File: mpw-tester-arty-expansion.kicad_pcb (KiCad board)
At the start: 4 copper layers, 53.3 x 61.5 mm, 140 parts, among them J1 USB4105-GF-A, J10 61300211121, J11 61300211121, J12 61300211121, J14 61300311121, J15 61300311121, J18 61300411121, J19 61300711121, J2 61300211121, J20 61300411121, J3 Arty_A7_SPI, J4 61300211121, J5 61300311121, J6 61300211121, J7 61300211121, J8 61300211121, J9 61300211121, Q1 DTC014TEBTL, U1 SN74LVC1G125DCKR, U2 FT232HQ, U3 SN74LVC1G125DCKR, U4 MAX811REUS+T, U5 NTS0102DP, U6 MCP4661-103E/ML, U7 Caravel_breakout_PCB, U8 W25Q32FVSS, U9 MIC2211-AAYML-TR, Y1 ABM8G-12.000MHZ-18-D2Y-T, Y2 ECS-2520MVLC-100-BN-TR

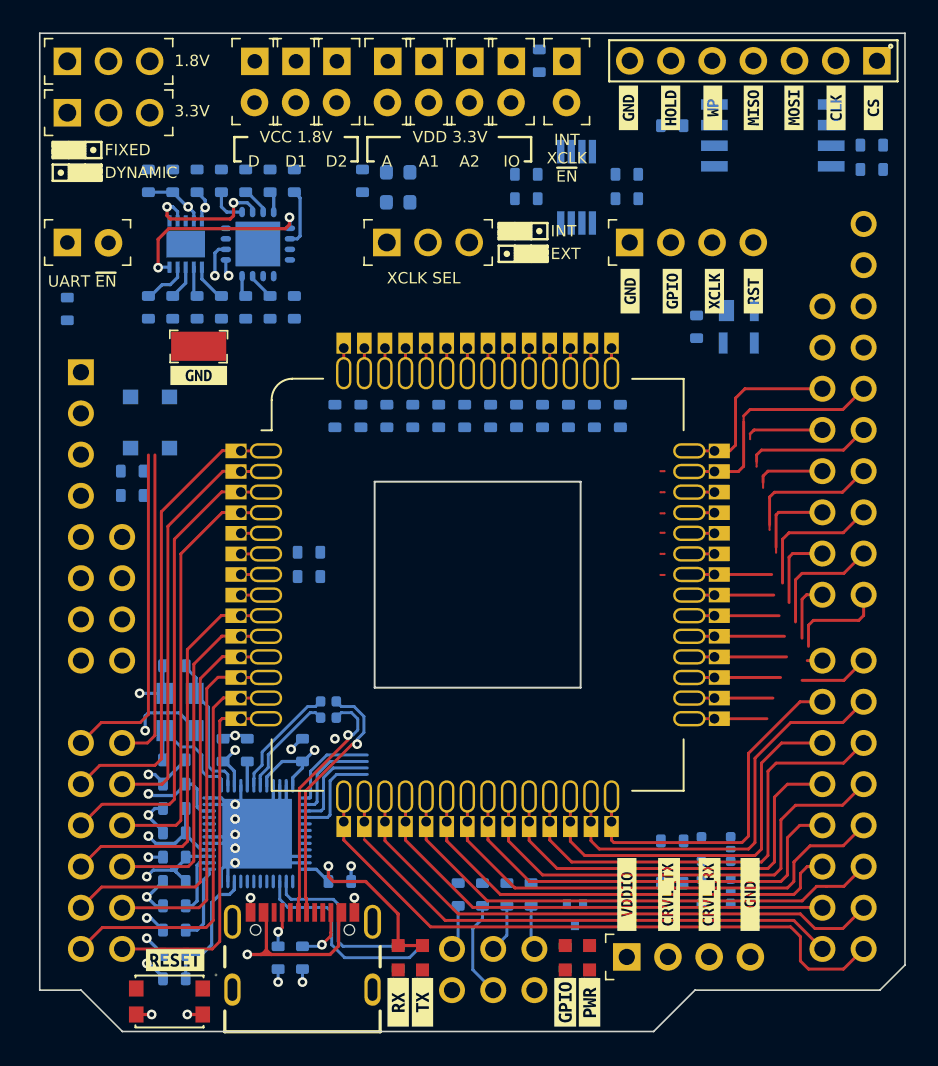
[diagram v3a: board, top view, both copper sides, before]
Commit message: Start power section layout. Adjust J6-J12 position on schematic to resolve crosses on PCB
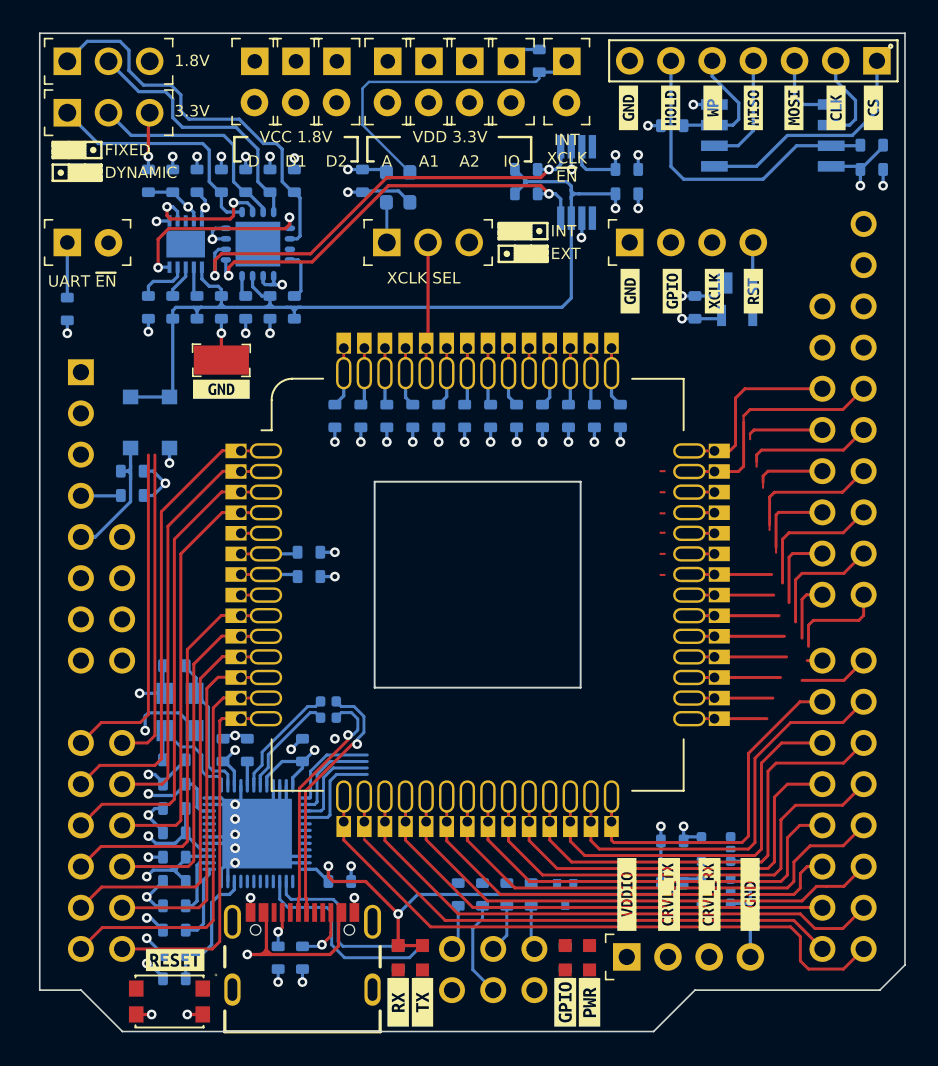
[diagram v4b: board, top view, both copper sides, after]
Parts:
- moved U4 1.70 mm to (166.0, 82.4)
- moved TP1 1.64 mm to (134.2, 86.2)
- moved kibuzzard-638FA1CB 1.64 mm to (134.2, 88.0)
- moved Q1 1.39 mm to (155.4, 119.1)
- moved C20 1.20 mm to (163.4, 82.9)
- moved C21 0.30 mm to (159.2, 74.4)
- moved C25 0.30 mm to (159.2, 75.9)
- moved R27 0.30 mm to (153.0, 74.4)
- moved R31 0.30 mm to (153.0, 75.9)
- moved U5 0.30 mm to (156.1, 75.2)
- turned C19 to -90 degrees
- turned R16 to 90 degrees
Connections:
- J3 pad 19: unconnected-(J3-Pad19) -> /EN_VOUT2
- J3 pad 31: unconnected-(J3-Pad31) -> /~{MR}
- J3 pad 32: unconnected-(J3-Pad32) -> /ARTY_XCLK
- J3 pad 9: unconnected-(J3-Pad9) -> /EN_VOUT1
- J6 pad 2: /VDDIO -> /VDDA
- J7 pad 2: /VDDA -> /VDDIO
- J8 pad 2: /VDDA1 -> /VDDA2
- J9 pad 2: /VDDA2 -> /VDDA1
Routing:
- net /3V3_ARTY: track 0.00 -> 56.9 mm, vias 0 -> 2
- net /5V0: track 4.03 -> 59.5 mm, vias 0 -> 1
- net AGND: track 74.4 -> 125.3 mm, vias 23 -> 52
- net /ARTY_SDA: track 2.17 -> 28.7 mm, vias 1 -> 2
- net VBUS: track 30.3 -> 56.6 mm, vias 2 -> 3
- net /ARTY_SCL: track 1.05 -> 26.3 mm, vias 1 -> 2
- net +3V3: track 2.06 -> 23.0 mm, vias 1 -> 13
- net unconnected-(J3-Pad9): track 20.9 -> 0.00 mm
- net /EN_VOUT1: track 1.86 -> 22.7 mm
- net /P0B: track 3.54 -> 24.4 mm
- net /XCLK_EN: track 0.00 -> 19.9 mm
- net /VDDIO: track 3.10 -> 22.9 mm
- net /FTDI_3V3: track 33.5 -> 53.1 mm, vias 6 -> 7
- net unconnected-(J3-Pad19): track 19.5 -> 0.00 mm
- net /EN_VOUT2: track 2.11 -> 21.6 mm
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- added copper zone on In2.Cu, net +1V8
- added copper zone on In2.Cu, net +3V3

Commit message: Import changes to PCB, place new diodes
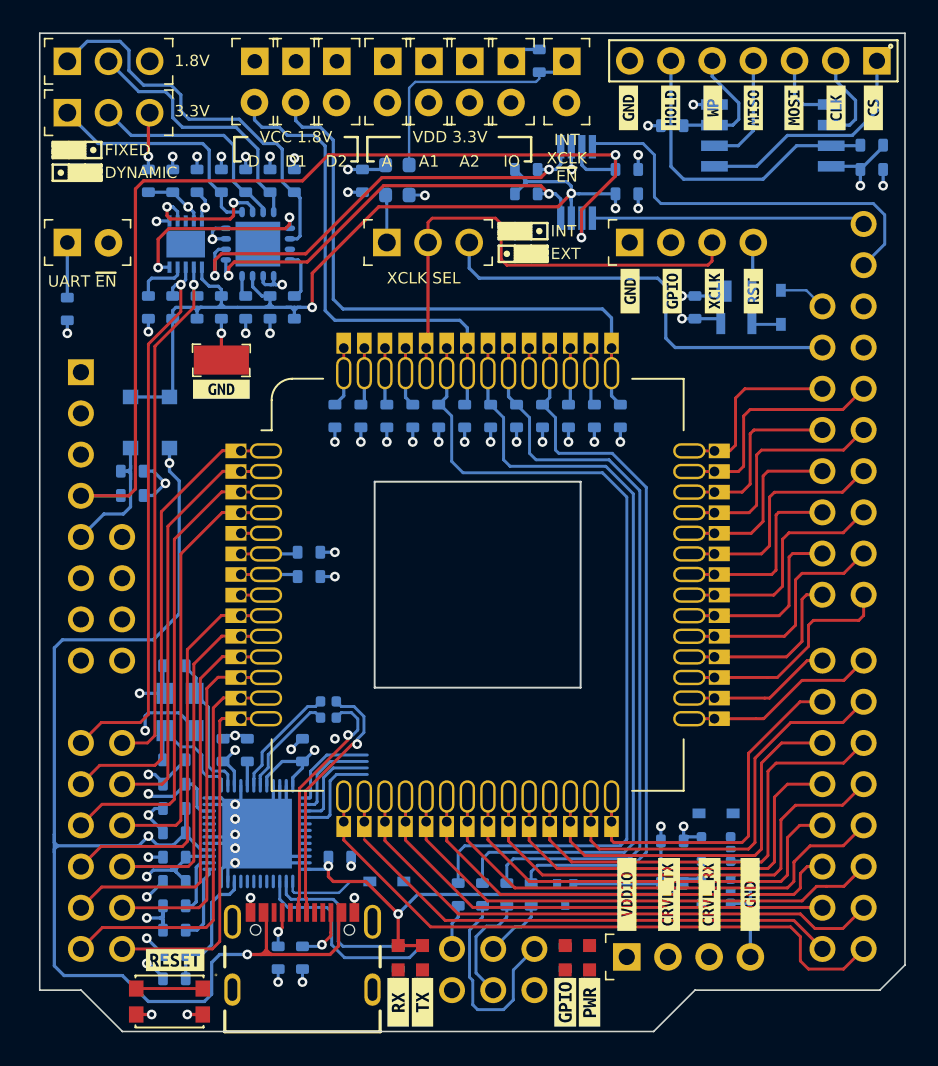
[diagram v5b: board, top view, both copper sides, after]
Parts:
- removed NT1, NT10, NT11, NT12, NT2, NT3, NT4, NT5, NT6, NT7, NT8, NT9: NetTie_2, antmicro-footprints:NetTie-2_SMD_Pad0.127mm
- added D7: 1N5819HW-7-F, antmicro-footprints:SOD-123, B.Cu at (131.0, 90.0)
- added D8: 1N5819HW-7-F, antmicro-footprints:SOD-123, B.Cu at (128.6, 90.0)
- added D9: PMEG6002EJ,115, antmicro-footprints:SOD-323F, B.Cu at (168.7, 82.9)
- D5, D6: value 1N5819HW-7-F -> PMEG6002EJ,115; footprint antmicro-footprints:SOD-123 -> antmicro-footprints:SOD-323F
- moved D5 41.4 mm to (164.7, 114.1), turned to 0 degrees
- moved D6 32.4 mm to (144.4, 118.3), turned to 0 degrees
- moved R14 3.00 mm to (150.3, 119.1)
- moved C16 1.50 mm to (141.5, 116.8)
- moved R11 1.50 mm to (153.3, 119.1)
- moved R15 1.50 mm to (151.8, 119.1)
- moved U4 0.50 mm to (165.9, 82.9)
- moved Y2 0.45 mm to (145.1, 75.0)
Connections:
- D5 pad A: VBUS -> /~{UART_EN}
- D5 pad K: /5V0 -> Net-(U2-Pad21)
- D6 pad A: /5V0_ARTY -> /~{MR}
- D6 pad K: /5V0 -> Net-(U2-Pad25)
- J18 pad 2: /CRVL_TX -> /CRVL_IO5
- J18 pad 3: /CRVL_RX -> /CRVL_IO6
- J3 pad 19: /EN_VOUT2 -> /EN_VOUT1
- J3 pad 31: /~{MR} -> Net-(J3-Pad31)
- J3 pad 34: /ARTY_MOSI -> /CRVL_IO2
- J3 pad 35: /ARTY_SCK -> /CRVL_IO4
- J3 pad 36: /ARTY_RX -> /CRVL_IO6
- J3 pad 51: /ARTY_MISO -> /CRVL_IO1
- J3 pad 52: /ARTY_CS -> /CRVL_IO3
- J3 pad 53: /ARTY_TX -> /CRVL_IO5
- J3 pad 9: /EN_VOUT1 -> /EN_VOUT2
- Q1 pad 1: /GPIO -> /CRVL_GPIO
- U2 pad 13: /USB_SCK_TXD -> /CRVL_IO4
- U2 pad 14: /USB_SO_RXD -> /CRVL_IO2
- U2 pad 15: /USB_SI -> /CRVL_IO1
- U2 pad 16: /USB_CS1 -> /CRVL_IO3
- U2 pad 21: /~{UART_EN} -> Net-(U2-Pad21)
- U2 pad 25: /~{MR} -> Net-(U2-Pad25)
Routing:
- net /MEM.~{CS}: track 18.2 -> 67.5 mm
- net /MEM.SI: track 8.19 -> 53.5 mm
- net /MEM.SO: track 10.8 -> 53.7 mm
- net /MEM.SCK: track 9.43 -> 49.9 mm
- net /VCCD1: track 3.72 -> 36.9 mm
- net /ARTY_XCLK: track 0.00 -> 27.3 mm
- net /VCCD: track 7.10 -> 33.8 mm
- net /ARTY_SDA_3V3: track 0.00 -> 25.1 mm
- net /VDDA1: track 3.58 -> 27.3 mm
- net /CRVL_XCLK: track 8.11 -> 30.7 mm
- net VBUS: track 56.6 -> 79.1 mm
- net /CRVL_IO3: track 1.55 -> 20.9 mm
- net /VDDA: track 3.54 -> 21.8 mm
- net /VDDIO: track 22.9 -> 40.3 mm
- net /ARTY_SCL_3V3: track 0.00 -> 16.9 mm
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
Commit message: Add PWR CTRL switch to the PCB, place UART selector in TMP place
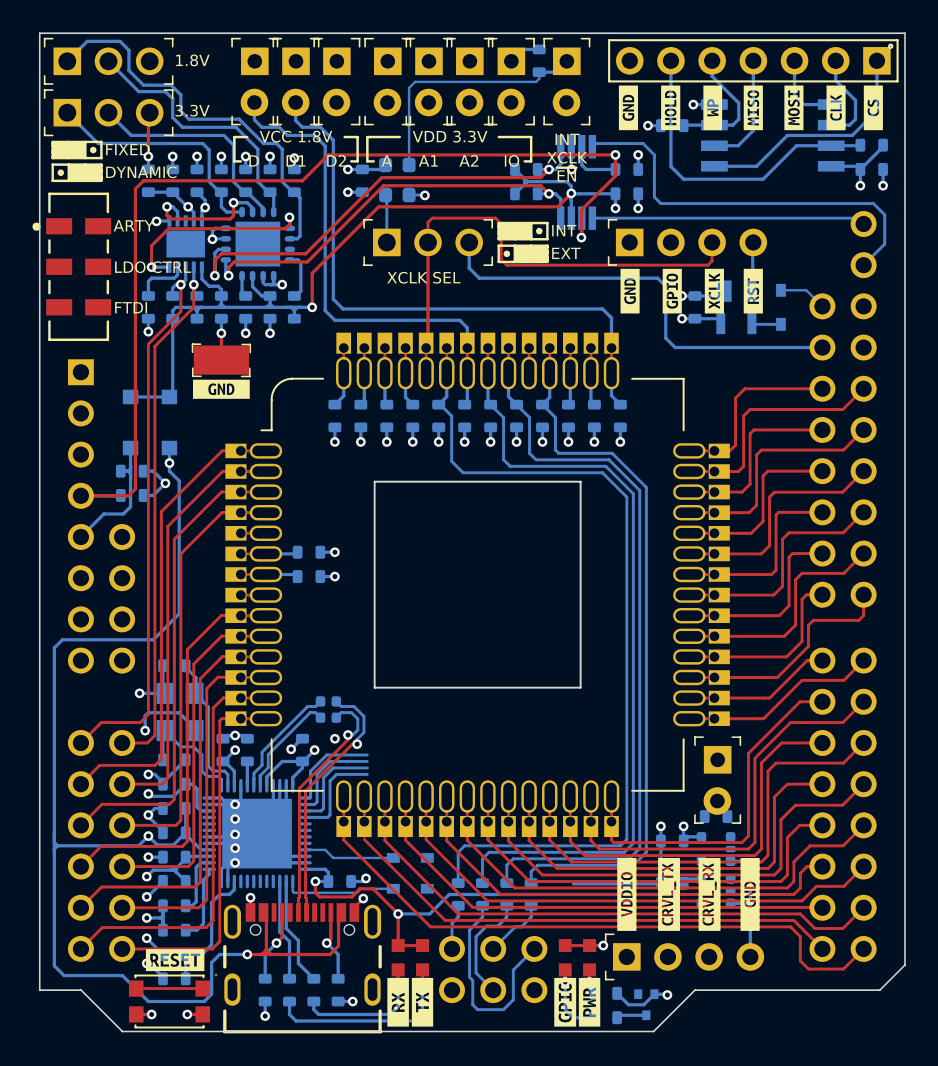
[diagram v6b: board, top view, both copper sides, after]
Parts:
- added SW1: JS202011JCQN, antmicro-footprints:JS202011JCQN, F.Cu at (125.4, 80.4)
- moved J2 51.2 mm to (164.8, 110.8), turned to -90 degrees
- moved R1 50.8 mm to (164.7, 114.3), turned to 180 degrees
- moved D5 19.0 mm to (145.8, 116.8)
- moved Q1 8.44 mm to (160.4, 125.9)
- moved R10 8.44 mm to (138.4, 125.0)
- moved R9 5.57 mm to (139.9, 125.0)
- moved R12 4.47 mm to (157.9, 126.7), turned to 180 degrees
- moved R3 2.97 mm to (141.4, 125.0)
- moved R13 2.42 mm to (157.9, 125.2), turned to 180 degrees
- moved R2 2.15 mm to (136.9, 125.0)
- moved D6 1.52 mm to (145.8, 118.8)
- moved C16 1.50 mm to (141.5, 118.3)
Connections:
- net Net-(J3-Pad31) renamed /ARTY_~{MR}
- net Net-(U2-Pad21) renamed /FTDI_~{UART_EN}
- net Net-(U2-Pad25) renamed /FTDI_~{MR}
- J3 pad 19: /EN_VOUT1 -> /ARTY_EN_VOUT1
- J3 pad 9: /EN_VOUT2 -> /ARTY_EN_VOUT2
- U1 pad 2: /USB_SCK_TXD -> /CRVL_IO4
- U2 pad 29: /EN_1V8 -> /FTDI_EN_VOUT1
- U2 pad 30: /EN_3V3 -> /FTDI_EN_VOUT2
- U3 pad 4: /USB_SO_RXD -> /CRVL_IO2
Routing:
- net Net-(D2-Pad2): track 0.00 -> 12.0 mm, vias 0 -> 1
- net Net-(D1-Pad2): track 0.00 -> 8.28 mm, vias 0 -> 1
- net /~{TX_LED}: track 12.9 -> 6.25 mm
- net /FTDI_~{UART_EN}: track 0.00 -> 5.66 mm
- net AGND: track 128.9 -> 133.4 mm
- net Net-(D3-Pad2): track 0.00 -> 4.46 mm, vias 0 -> 1
- net /~{RX_LED}: track 10.4 -> 6.70 mm, vias 0 -> 1
- net /~{UART_EN}: track 3.40 -> 0.00 mm
- net /CC1: track 2.19 -> 4.52 mm
- net /FTDI_3V3: track 52.0 -> 54.2 mm
- net Net-(Q1-Pad3): track 0.00 -> 1.86 mm
- net Net-(D4-Pad2): track 0.00 -> 1.57 mm, vias 0 -> 1
- net +3V3: track 23.0 -> 24.6 mm
- net /FTDI_~{MR}: track 5.68 -> 6.94 mm
- net /CC2: track 3.46 -> 4.48 mm
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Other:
- board text added: "ARTY"
- board text added: "FTDI"
- board text added: "LDO CTRL"
- board text removed: "UART ~{EN}"

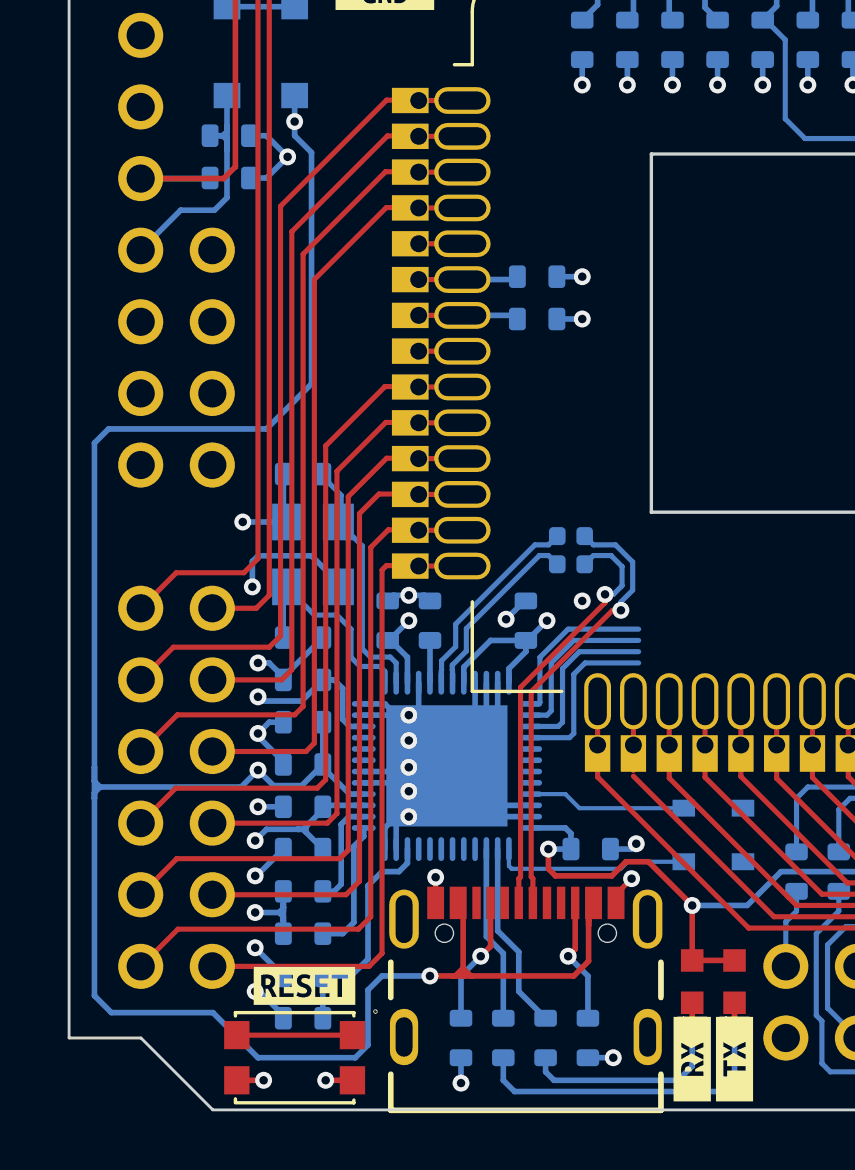
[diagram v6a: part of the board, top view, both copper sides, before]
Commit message: correct too small footprint of FTDI, reconnect nearby tracks
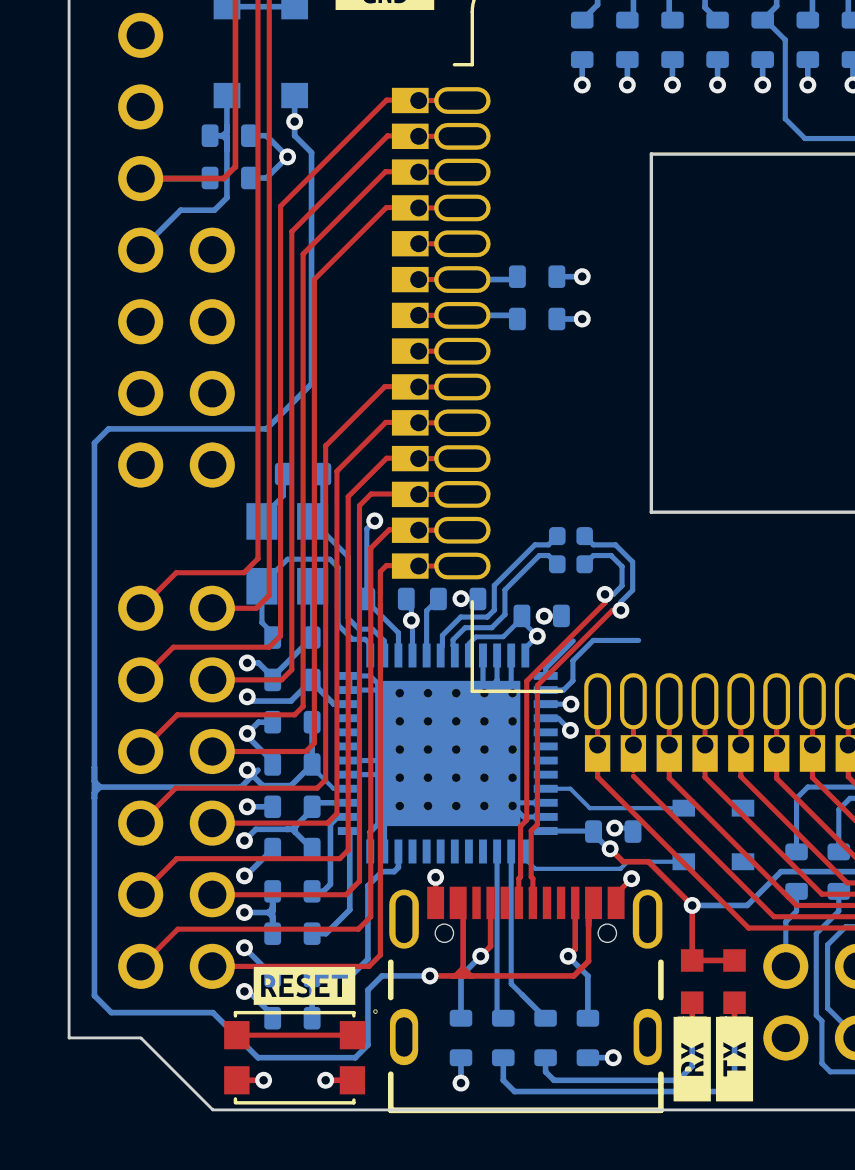
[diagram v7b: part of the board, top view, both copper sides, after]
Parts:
- U2: footprint antmicro-footprints:QFN-48-1EP_6x6mm -> antmicro-footprints:QFN-48-1EP_7x7mm
- moved R7 1.26 mm to (136.8, 109.4), turned to 180 degrees
- moved C16 1.01 mm to (142.3, 117.7)
- moved Y1 0.91 mm to (130.8, 107.9)
- moved C5 0.77 mm to (134.3, 109.4), turned to 0 degrees
- moved C8 0.59 mm to (139.8, 110.0), turned to 0 degrees
- moved U2 0.44 mm to (136.4, 114.9)
- moved C11 0.38 mm to (130.9, 119.8)
- moved C12 0.38 mm to (130.9, 116.8)
- moved C14 0.38 mm to (130.9, 121.3)
- moved C15 0.38 mm to (130.9, 118.3)
- moved C17 0.38 mm to (130.9, 122.8)
- moved C2 0.38 mm to (130.9, 113.8)
- moved C4 0.38 mm to (130.9, 112.3)
- moved C6 0.38 mm to (130.9, 110.8)
- moved C7 0.38 mm to (130.9, 115.3)
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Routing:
- net AGND: track 133.4 -> 117.3 mm, vias 53 -> 47
- net /CRVL_IO1: track 20.7 -> 15.6 mm, vias 0 -> 1
- net /CRVL_IO3: track 20.9 -> 15.7 mm, vias 0 -> 1
- net /CRVL_IO4: track 17.3 -> 13.1 mm
- net /FTDI_3V3: track 54.2 -> 50.8 mm
- net /XIN: track 7.61 -> 9.14 mm
- net /CRVL_IO2: track 17.6 -> 16.1 mm
- net /XOUT: track 8.93 -> 7.92 mm
- net /FTDI_~{MR}: track 6.94 -> 6.13 mm
- net /REF: track 1.45 -> 2.11 mm
- net /VCCA: track 5.01 -> 4.48 mm
- net /~{RX_LED}: track 6.70 -> 6.42 mm, vias 1 -> 0
